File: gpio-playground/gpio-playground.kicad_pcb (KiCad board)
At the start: 2 copper layers, 46.7 x 42.2 mm, 42 parts, among them J1 Conn_02x03_Odd_Even, J2 Conn_02x08_Odd_Even, SW1 SW_Push, SW2 SW_Push, SW3 SW_Push, SW4 SW_Push, SW5 SW_Push, SW6 SW_Push, SW7 SW_Push, SW8 SW_Push, U1 BIWIN_DTS04GE_SMD, U2 BIWIN_DTS04GE_SMD, U3 74AHC244

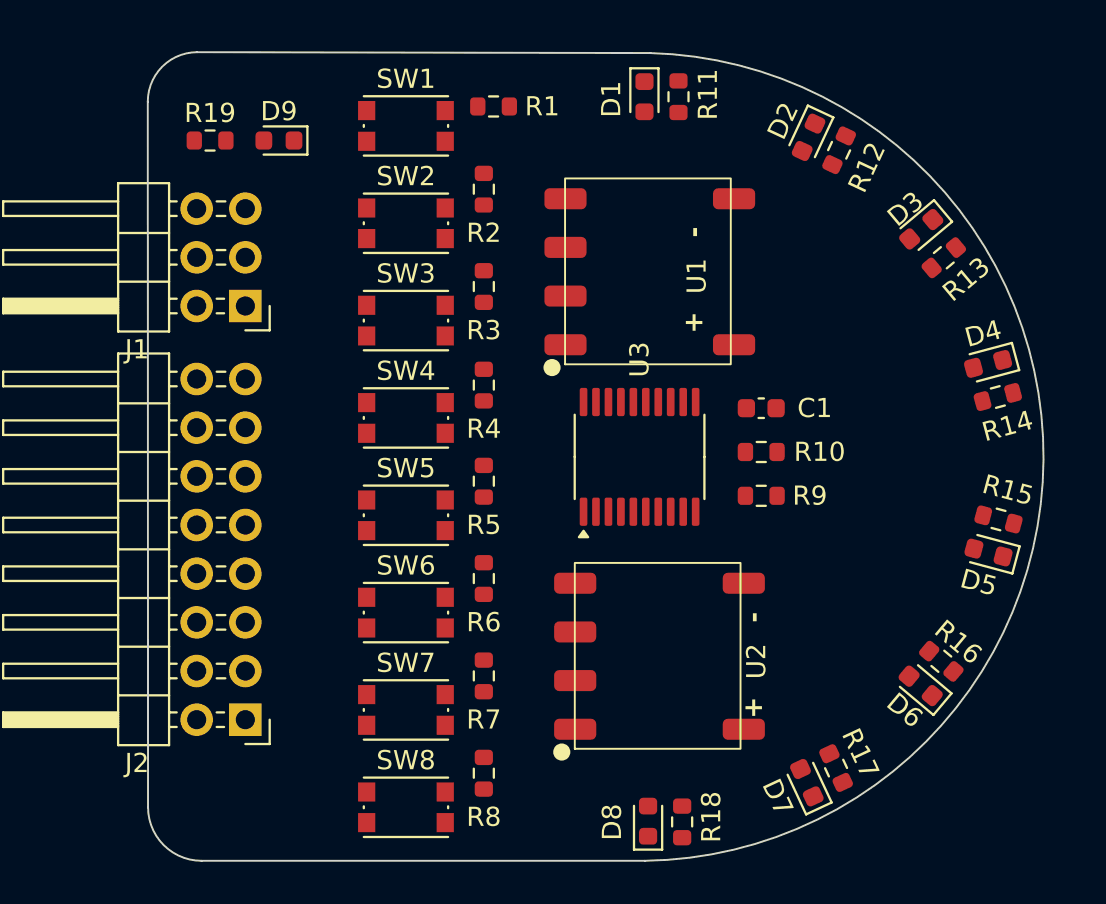
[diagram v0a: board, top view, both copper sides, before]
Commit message: Added gpio playground PCB
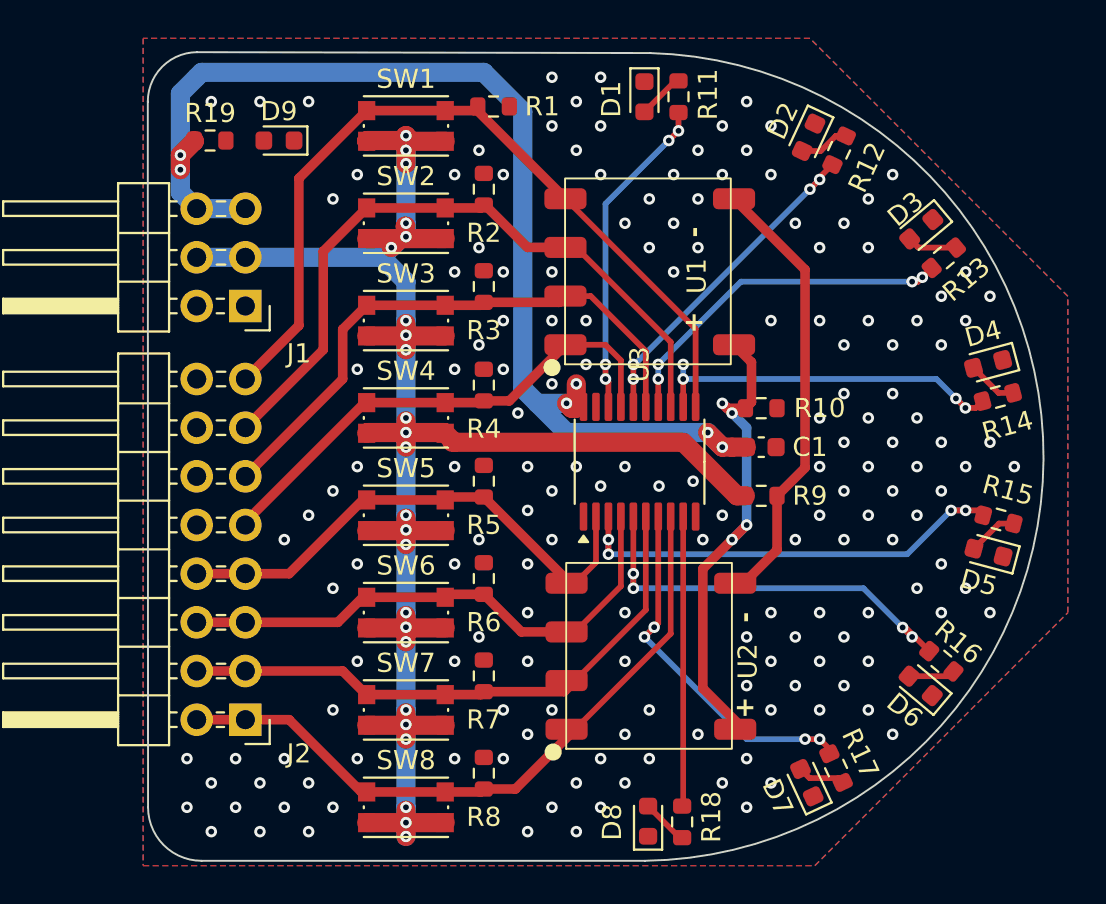
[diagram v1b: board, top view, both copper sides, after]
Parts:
- moved R10 2.29 mm to (73.2, 94.7), turned to 180 degrees
- moved C1 2.03 mm to (73.2, 96.8), turned to 180 degrees
- moved U2 0.45 mm to (69.6, 111.5)
- moved U3 0.25 mm to (66.8, 97.5)
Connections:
- U2 pad 1: /DMUX_4 -> /DMUX_7
- U2 pad 2: /DMUX_5 -> /DMUX_6
- U2 pad 3: /DMUX_6 -> /DMUX_5
- U2 pad 4: /DMUX_7 -> /DMUX_4
- U3 pad 2: /DMUX_7 -> /DMUX_4
- U3 pad 4: /DMUX_6 -> /DMUX_5
- U3 pad 6: /DMUX_5 -> /DMUX_6
- U3 pad 8: /DMUX_4 -> /DMUX_7
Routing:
- net /VDDIO: track 0.00 -> 112.4 mm, vias 0 -> 24
- net /3V3: track 0.00 -> 61.8 mm, vias 0 -> 6
- net /DMUX_0: track 0.00 -> 42.7 mm
- net /DMUX_1: track 0.00 -> 36.1 mm
- net /DMUX_7: track 0.00 -> 36.1 mm
- net /DMUX_6: track 0.00 -> 30.9 mm
- net /DMUX_2: track 0.00 -> 30.2 mm
- net /DMUX_5: track 0.00 -> 28.4 mm
- net /DMUX_4: track 0.00 -> 27.5 mm
- net Net-(U1-+): track 0.00 -> 26.3 mm, vias 0 -> 4
- net /DMUX_3: track 0.00 -> 26.1 mm
- net Net-(U3-2Y0): track 0.00 -> 24.4 mm, vias 0 -> 4
- net Net-(U3-2Y1): track 0.00 -> 23.0 mm, vias 0 -> 4
- net Net-(U1--): track 0.00 -> 22.9 mm
- net Net-(U3-2Y2): track 0.00 -> 20.6 mm, vias 0 -> 4
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- added copper zone on B.Cu, net GND
- added copper zone on F.Cu, net GND

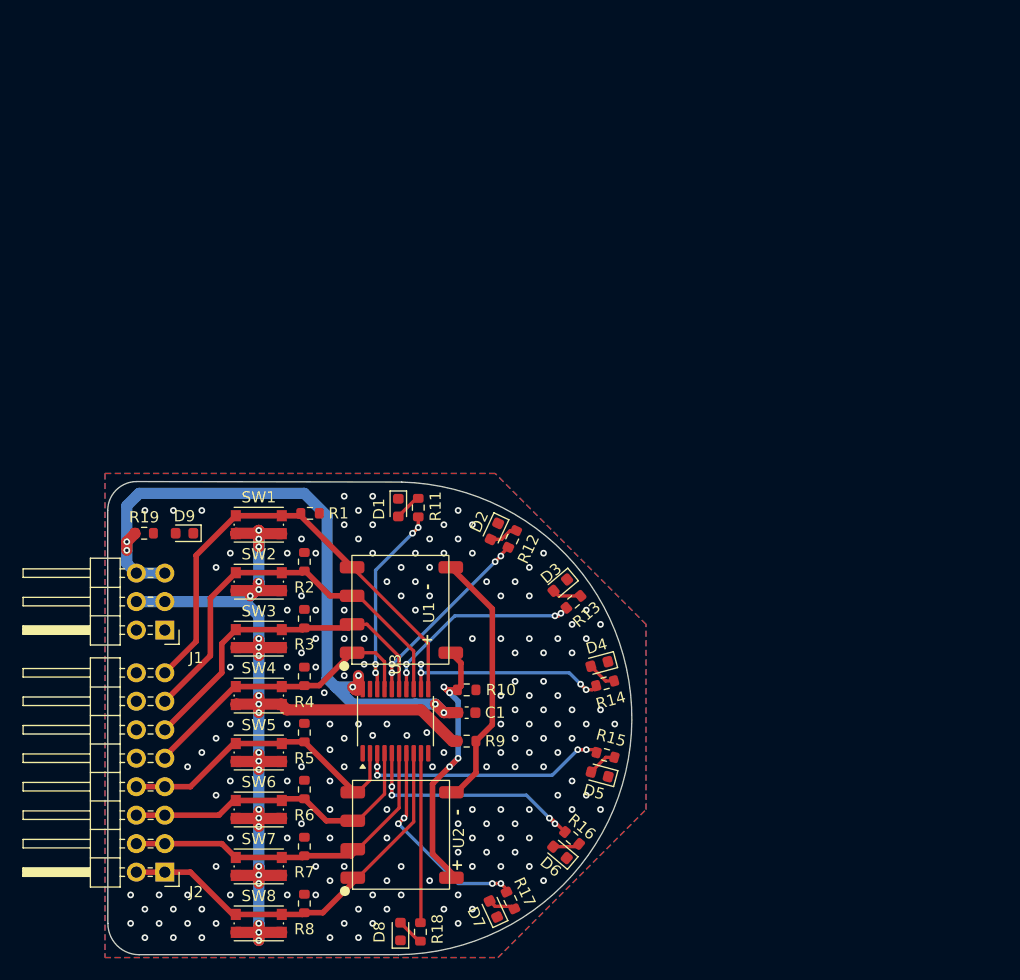
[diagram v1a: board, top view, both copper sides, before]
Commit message: Updated connector on bo
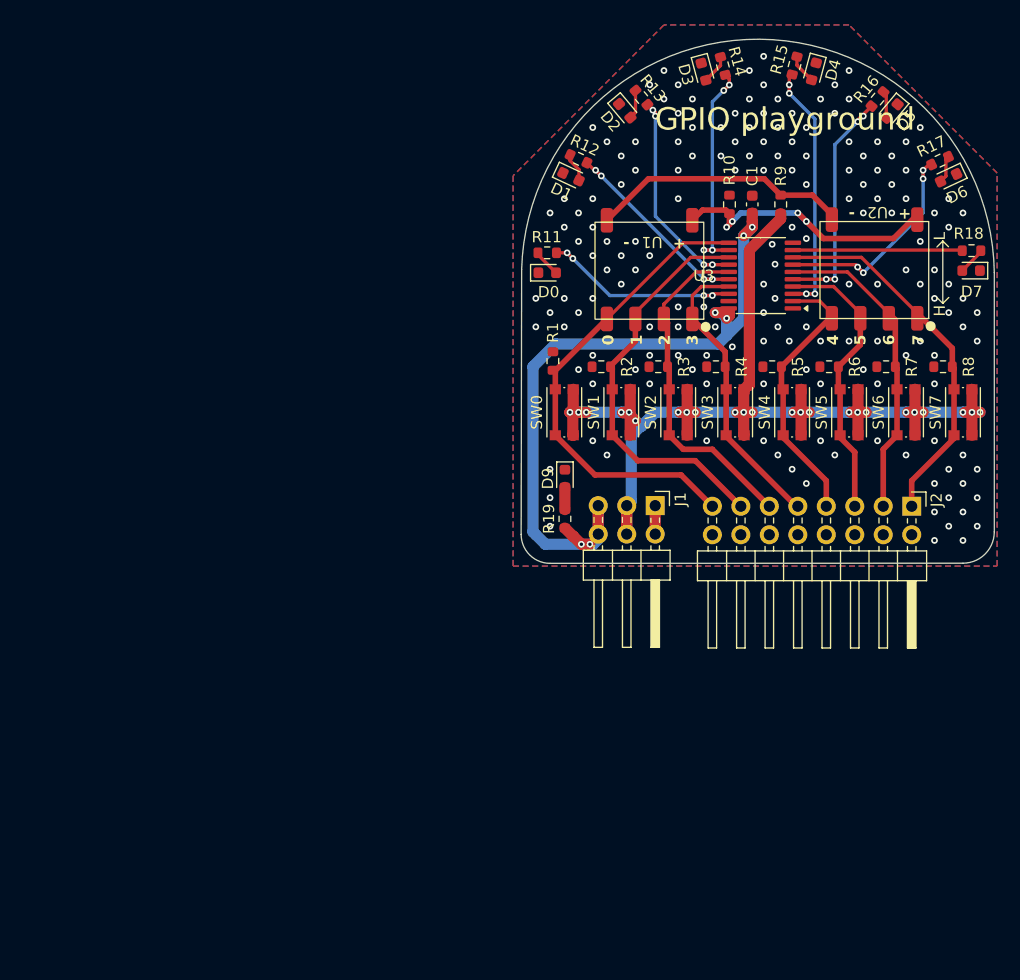
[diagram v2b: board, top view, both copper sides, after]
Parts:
- moved R18 78.2 mm to (118.2, 55.6), turned to 0 degrees
- moved D7 77.9 mm to (118.1, 57.3), turned to 180 degrees
- moved SW7 77.6 mm to (117.4, 70.0), turned to 90 degrees
- moved D6 76.8 mm to (116.1, 49.1), turned to -155 degrees
- moved R17 76.3 mm to (115.4, 47.5), turned to 25 degrees
- moved R8 74.4 mm to (115.6, 65.9), turned to 180 degrees
- moved J2 74.2 mm to (112.8, 78.4), turned to -90 degrees
- moved D5 72.4 mm to (111.1, 43.1), turned to -130 degrees
- moved U2 71.5 mm to (113.3, 55.0), turned to 180 degrees
- moved R16 71.3 mm to (109.8, 42.0), turned to 50 degrees
- moved SW6 70.5 mm to (112.3, 70.0), turned to 90 degrees
- moved R7 67.3 mm to (110.6, 65.9), turned to 180 degrees
- moved D4 65.5 mm to (104.1, 39.6), turned to -105 degrees
- moved R15 63.8 mm to (102.4, 39.1), turned to 75 degrees
- moved SW5 63.5 mm to (107.3, 70.0), turned to 90 degrees
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- renumbered D1 to D0, D2 to D1, D3 to D2, D4 to D3, D5 to D4, D6 to D5, D7 to D6, D8 to D7, SW1 to SW0, SW2 to SW1, SW3 to SW2, SW4 to SW3, SW5 to SW4, SW6 to SW5, SW7 to SW6, SW8 to SW7
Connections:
- J2 pad 10: /DMUX_3 -> unconnected-(J2-Pin_10-Pad10)
- J2 pad 12: /DMUX_2 -> unconnected-(J2-Pin_12-Pad12)
- J2 pad 14: /DMUX_1 -> unconnected-(J2-Pin_14-Pad14)
- J2 pad 16: /DMUX_0 -> unconnected-(J2-Pin_16-Pad16)
- J2 pad 2: /DMUX_7 -> unconnected-(J2-Pin_2-Pad2)
- J2 pad 4: /DMUX_6 -> unconnected-(J2-Pin_4-Pad4)
- J2 pad 6: /DMUX_5 -> unconnected-(J2-Pin_6-Pad6)
- J2 pad 8: /DMUX_4 -> unconnected-(J2-Pin_8-Pad8)
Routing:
- net /3V3: track 61.8 -> 65.6 mm
- net /VDDIO: track 112.4 -> 115.4 mm
- net /DMUX_4: track 27.5 -> 24.9 mm
- net /DMUX_5: track 28.4 -> 25.9 mm
- net GND: track 0.00 -> 2.54 mm, vias 168 -> 167
- net /DMUX_7: track 36.1 -> 33.5 mm
- net /DMUX_6: track 30.9 -> 28.4 mm
- net Net-(D9-A): track 0.00 -> 1.98 mm
- net Net-(U3-1Y1): track 17.5 -> 18.2 mm
- net Net-(U3-1Y3): track 19.1 -> 19.8 mm
- net Net-(U3-1Y2): track 18.9 -> 19.7 mm
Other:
- board size 46.7 x 42.2 mm -> 42.2 x 46.7 mm
- board text added: "0"
- board text added: "1"
- board text added: "2"
- board text added: "3"
- board text added: "4"
- board text added: "5"
- board text added: "6"
- board text added: "7"
- board text added: "GPIO playground"
- board text added: "H"
- board text added: "L"

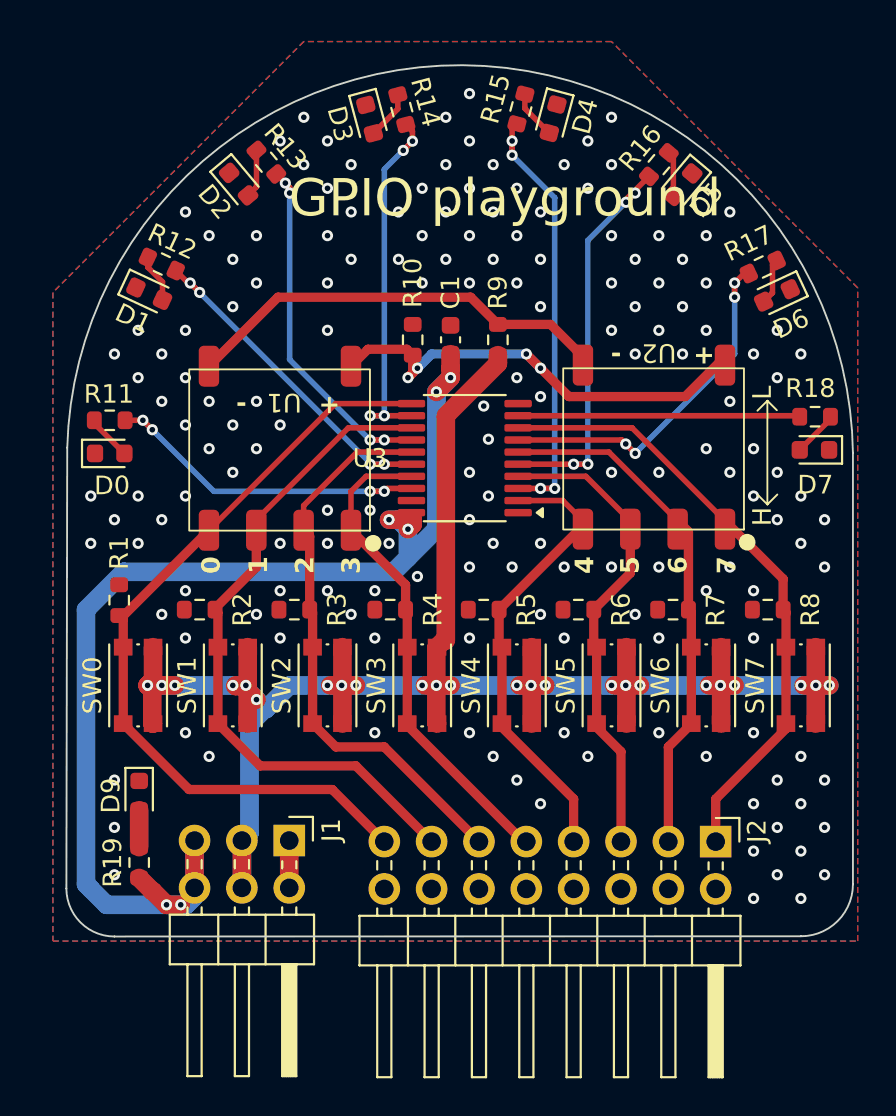
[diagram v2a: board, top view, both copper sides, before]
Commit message: Corrected the pin connections of the playground
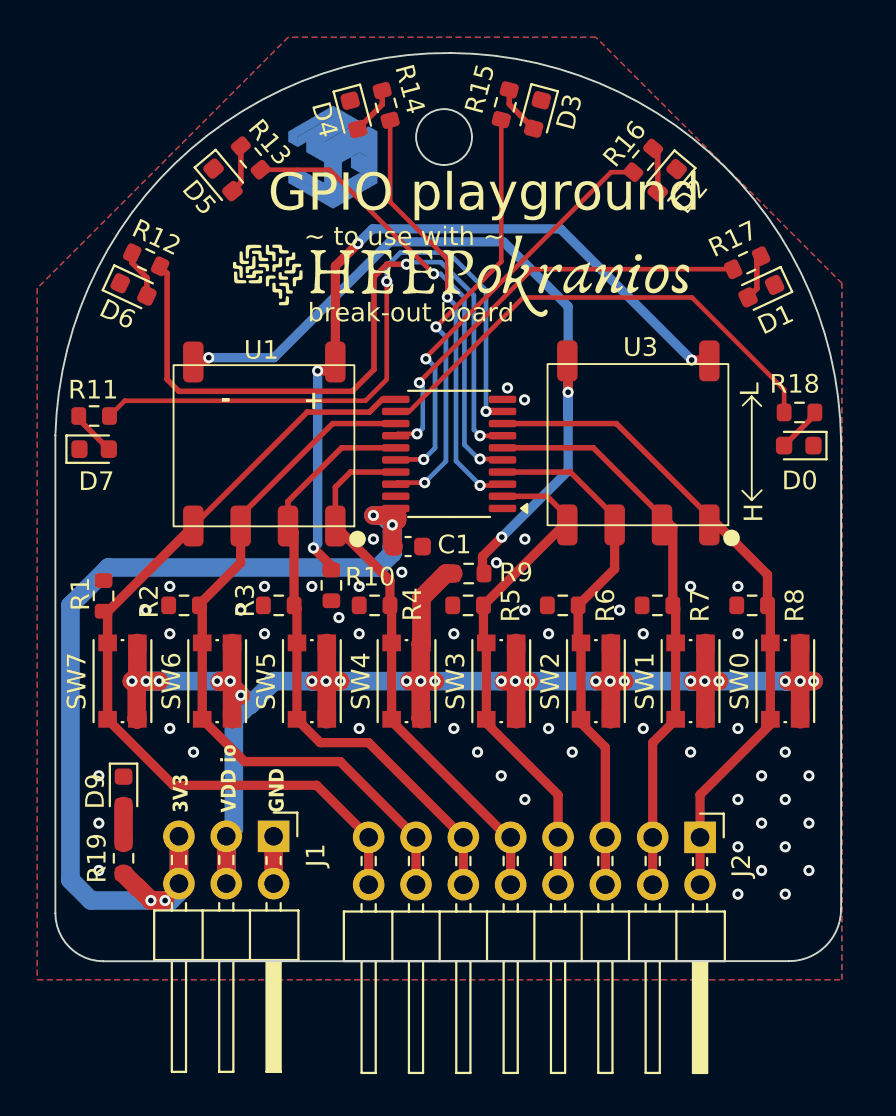
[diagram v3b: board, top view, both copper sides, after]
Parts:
- added ?: , clipboard:399e21bd-28b7-4f61-ba82-54584e613d6e, F.Cu at (98.3, 40.6)
- added G***: LOGO, LOGO, F.Cu at (99.2, 48.0)
- added G***: LOGO, LOGO, B.Cu at (100.7, 45.9)
- added G***: LOGO, LOGO, B.Cu at (104.3, 41.8)
- added REF**: ESL small, ESL-EPFL:ESL small, B.Cu at (91.9, 46.2)
- moved R10 13.9 mm to (92.2, 64.6), turned to 90 degrees
- moved R9 12.6 mm to (99.6, 64.0), turned to 0 degrees
- moved C1 11.3 mm to (96.3, 62.5), turned to 180 degrees
- moved D0 0.87 mm to (117.3, 57.1)
- moved D1 0.87 mm to (115.3, 48.8)
- moved D2 0.87 mm to (110.2, 42.9)
- moved D3 0.87 mm to (103.3, 39.4)
- moved D4 0.87 mm to (93.4, 39.4)
- moved D5 0.87 mm to (86.4, 42.9)
- moved D7 0.87 mm to (79.5, 57.3)
- moved D9 0.87 mm to (81.1, 75.7)
- moved J1 0.87 mm to (89.1, 78.1)
- moved J2 0.87 mm to (112.0, 78.1)
- moved R1 0.87 mm to (80.0, 65.2)
- moved R12 0.87 mm to (82.3, 47.1)
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- renumbered D7 to D0, D6 to D1, D5 to D2, D4 to D3, D3 to D4, D2 to D5, D1 to D6, D0 to D7, SW7 to SW0, SW6 to SW1, SW5 to SW2, SW4 to SW3, SW3 to SW4, SW2 to SW5, SW1 to SW6, SW0 to SW7
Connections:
- J2 pad 1: /DMUX_7 -> /DMUX_0
- J2 pad 11: /DMUX_2 -> /DMUX_5
- J2 pad 13: /DMUX_1 -> /DMUX_6
- J2 pad 15: /DMUX_0 -> /DMUX_7
- J2 pad 3: /DMUX_6 -> /DMUX_1
- J2 pad 5: /DMUX_5 -> /DMUX_2
- J2 pad 7: /DMUX_4 -> /DMUX_3
- J2 pad 9: /DMUX_3 -> /DMUX_4
- R1 pad 1: /DMUX_0 -> /DMUX_7
- R11 pad 1: Net-(U3-1Y0) -> Net-(U3-2Y3)
- R12 pad 1: Net-(U3-1Y1) -> Net-(U3-2Y2)
- R13 pad 1: Net-(U3-1Y2) -> Net-(U3-2Y1)
- R14 pad 1: Net-(U3-1Y3) -> Net-(U3-2Y0)
- R15 pad 1: Net-(U3-2Y0) -> Net-(U3-1Y0)
- R16 pad 1: Net-(U3-2Y1) -> Net-(U3-1Y1)
- R17 pad 1: Net-(U3-2Y2) -> Net-(U3-1Y2)
- R18 pad 1: Net-(U3-2Y3) -> Net-(U3-1Y3)
- R2 pad 1: /DMUX_1 -> /DMUX_6
- R3 pad 1: /DMUX_2 -> /DMUX_5
- R4 pad 1: /DMUX_3 -> /DMUX_4
- R5 pad 1: /DMUX_4 -> /DMUX_3
- R6 pad 1: /DMUX_5 -> /DMUX_2
- R7 pad 1: /DMUX_6 -> /DMUX_1
- R8 pad 1: /DMUX_7 -> /DMUX_0
- SW0 pad 1: /DMUX_7 -> /DMUX_0
- SW1 pad 1: /DMUX_6 -> /DMUX_1
- SW2 pad 1: /DMUX_5 -> /DMUX_2
- SW3 pad 1: /DMUX_4 -> /DMUX_3
- SW4 pad 1: /DMUX_3 -> /DMUX_4
- SW5 pad 1: /DMUX_2 -> /DMUX_5
- SW6 pad 1: /DMUX_1 -> /DMUX_6
- SW7 pad 1: /DMUX_0 -> /DMUX_7
- U1 pad 1: /DMUX_3 -> /DMUX_4
- U1 pad 2: /DMUX_2 -> /DMUX_5
- U1 pad 3: /DMUX_1 -> /DMUX_6
- U1 pad 4: /DMUX_0 -> /DMUX_7
- U2 pad 1: /DMUX_7 -> /DMUX_0
- U2 pad 2: /DMUX_6 -> /DMUX_1
- U2 pad 3: /DMUX_5 -> /DMUX_2
- U2 pad 4: /DMUX_4 -> /DMUX_3
- U3 pad 11: /DMUX_0 -> /DMUX_7
- U3 pad 13: /DMUX_1 -> /DMUX_6
- U3 pad 15: /DMUX_2 -> /DMUX_5
- U3 pad 17: /DMUX_3 -> /DMUX_4
- U3 pad 2: /DMUX_4 -> /DMUX_3
- U3 pad 4: /DMUX_5 -> /DMUX_2
- U3 pad 6: /DMUX_6 -> /DMUX_1
- U3 pad 8: /DMUX_7 -> /DMUX_0
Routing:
- net Net-(U1--): track 22.9 -> 43.5 mm, vias 0 -> 3
- net Net-(U3-2Y3): track 15.4 -> 35.6 mm, vias 0 -> 2
- net Net-(U3-2Y2): track 20.6 -> 38.3 mm, vias 4 -> 2
- net Net-(U1-+): track 26.3 -> 41.3 mm
- net /VDDIO: track 115.4 -> 103.1 mm
- net /DMUX_7: track 33.5 -> 45.2 mm
- net /3V3: track 65.6 -> 55.0 mm, vias 6 -> 4
- net /DMUX_6: track 28.4 -> 38.7 mm
- net Net-(U3-1Y3): track 19.8 -> 27.1 mm, vias 4 -> 0
- net /DMUX_5: track 25.9 -> 32.7 mm
- net /DMUX_0: track 42.7 -> 36.1 mm
- net /DMUX_1: track 36.1 -> 30.9 mm
- net Net-(U3-1Y0): track 18.2 -> 23.2 mm, vias 4 -> 2
- net Net-(U3-1Y1): track 18.2 -> 22.7 mm, vias 4 -> 2
- net Net-(U3-1Y2): track 19.7 -> 23.5 mm, vias 4 -> 2
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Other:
- board size 42.2 x 46.7 mm -> 42.2 x 48.7 mm
- board text added: "3V3 VDD io GND"
- board text added: "GPIO playground v1.0 July 2026"
- board text added: "break-out board"
- board text added: "~ to use with ~"
- board text removed: "0"
- board text removed: "1"
- board text removed: "2"
- board text removed: "3"
- board text removed: "4"
- board text removed: "5"
- board text removed: "6"
- board text removed: "7"
